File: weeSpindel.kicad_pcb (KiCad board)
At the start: 2 copper layers, 107.9 x 17.8 mm, 23 parts, among them J1 MPU-6050, SW1 POWER, U1 ESP-12E, U2 HT7733SA, U3 MCP1700-3302E_SOT23

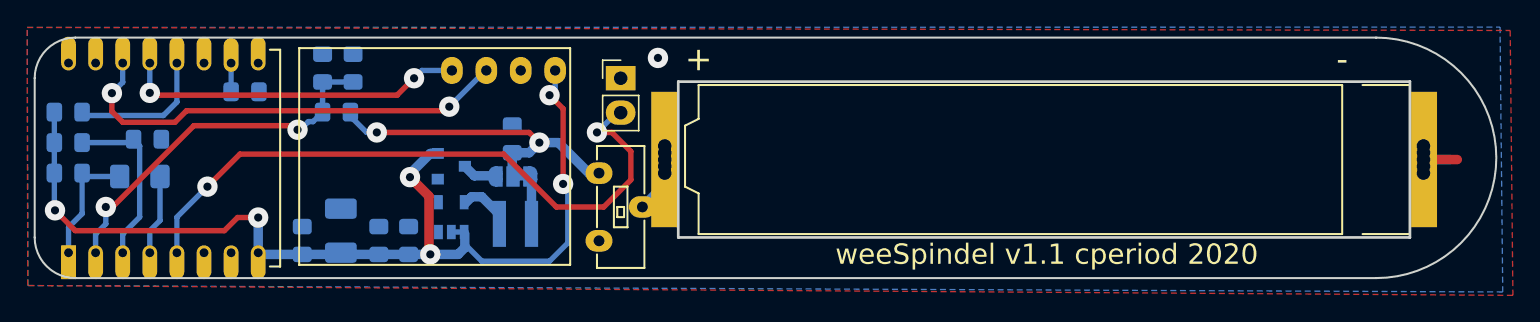
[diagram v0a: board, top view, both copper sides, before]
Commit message: the spring on the negative is a bit looser than necessary, allowing us to shave 2mm off our overall length
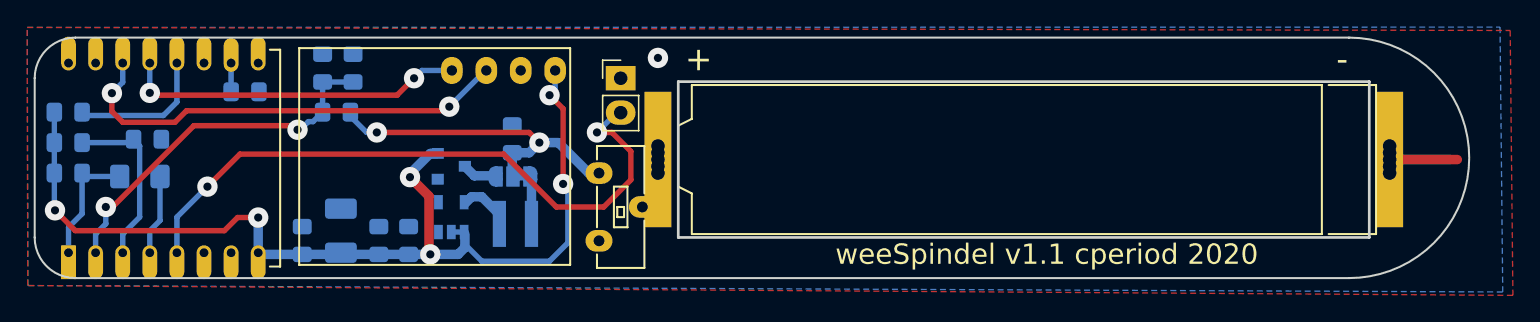
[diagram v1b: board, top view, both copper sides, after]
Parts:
- moved BT1 1.50 mm to (164.0, 105.0)
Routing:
- net GND: track 4.50 -> 9.71 mm
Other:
- board size 107.9 x 17.8 mm -> 105.9 x 17.8 mm
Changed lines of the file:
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@@
     (thickness 1.6)
     (drawings 16)
-    (tracks 139)
+    (tracks 140)
     (zones 0)
     (modules 23)
@@
     (add_net SDA)
   )
+  (module CPB:Battery_Springs_AAA (layer F.Cu)
+    (at 164 105)
+    (fp_text reference BT1 (at 30.5 0 90) (layer F.SilkS) hide
+      (effects (font (size 1 1) (thickness 0.15)))
+    )
+    (fp_text value NiMH (at 0 -9.271) (layer F.Fab)
+      (effects (font (size 1 1) (thickness 0.15)))
+    )
+    (fp_line (start 22 -5.5) (end -24.5 -5.5) (layer F.SilkS) (width 0.15))
+    (fp_line (start -24.5 -5.5) (end -24.5 -3) (layer F.SilkS) (width 0.15))
+    (fp_line (start -24.5 -3) (end -25.5 -2.5) (layer F.SilkS) (width 0.15))
+    (fp_line (start -25.5 -2.5) (end -25.5 2) (layer F.SilkS) (width 0.15))
+    (fp_line (start -25.5 2) (end -24.5 2.5) (layer F.SilkS) (width 0.15))
+    (fp_line (start -24.5 2.5) (end -24.5 5.5) (layer F.SilkS) (width 0.15))
+    (fp_line (start -24.5 5.5) (end 22 5.5) (layer F.SilkS) (width 0.15))
+    (fp_line (start 22 5.5) (end 22 -5.5) (layer F.SilkS) (width 0.15))
+    (fp_line (start 22.5 -5.5) (end 26 -5.5) (layer F.SilkS) (width 0.15))
+    (fp_line (start 26 -5.5) (end 26 5.5) (layer F.SilkS) (width 0.15))
+    (fp_line (start 26 5.5) (end 22.5 5.5) (layer F.SilkS) (width 0.15))
+    (fp_line (start 29 -6) (end -28.5 -6) (layer F.Fab) (width 0.15))
+    (fp_line (start -28.5 -6) (end -28.5 6) (layer F.Fab) (width 0.15))
+    (fp_line (start -28.5 6) (end 29 6) (layer F.Fab) (width 0.15))
+    (fp_line (start 29 6) (end 29 -6) (layer F.Fab) (width 0.15))
+    (pad 2 thru_hole circle (at 27 1) (size 1 1) (drill 1) (layers *.Cu *.Mask)
+      (net 1 GND))
+    (pad 2 thru_hole circle (at 27 0.5) (size 1 1) (drill 1) (layers *.Cu *.Mask)
+      (net 1 GND))
+    (pad 2 thru_hole circle (at 27 -1) (size 1 1) (drill 1) (layers *.Cu *.Mask)
+      (net 1 GND))
+    (pad 2 thru_hole circle (at 27 -0.5) (size 1 1) (drill 1) (layers *.Cu *.Mask)
+      (net 1 GND))
+    (pad 1 thru_hole circle (at -27 -0.5) (size 1 1) (drill 1) (layers *.Cu *.Mask)
+      (net 8 "Net-(BT1-Pad1)"))
+    (pad 1 thru_hole circle (at -27 0.5) (size 1 1) (drill 1) (layers *.Cu *.Mask)
+      (net 8 "Net-(BT1-Pad1)"))
+    (pad 1 thru_hole circle (at -27 1) (size 1 1) (drill 1) (layers *.Cu *.Mask)
+      (net 8 "Net-(BT1-Pad1)"))
+    (pad 1 thru_hole circle (at -27 -1) (size 1 1) (drill 1) (layers *.Cu *.Mask)
+      (net 8 "Net-(BT1-Pad1)"))
+    (pad 2 thru_hole rect (at 27 0) (size 2 10) (drill 1) (layers *.Cu *.Mask)
+      (net 1 GND))
+    (pad 1 thru_hole rect (at -27 0) (size 2 10) (drill 1) (layers *.Cu *.Mask)
+      (net 8 "Net-(BT1-Pad1)"))
+  )
   (module Jumper:SolderJumper-3_P1.3mm_Bridged12_RoundedPad1.0x1.5mm (layer B.Cu)
     (at 126.3 106.25 180)
@@
     )
   )
-  (module CPB:Battery_Springs_AAA (layer F.Cu)
-    (at 165.5 105)
-    (fp_text reference BT1 (at 30.5 0 90) (layer F.SilkS) hide
-      (effects (font (size 1 1) (thickness 0.15)))
-    )
-    (fp_text value NiMH (at 0 -9.271) (layer F.Fab)
-      (effects (font (size 1 1) (thickness 0.15)))
-    )
-    (fp_line (start 22 -5.5) (end -25.5 -5.5) (layer F.SilkS) (width 0.15))
-    (fp_line (start -25.5 -5.5) (end -25.5 -3) (layer F.SilkS) (width 0.15))
-    (fp_line (start -25.5 -3) (end -26.5 -2.5) (layer F.SilkS) (width 0.15))
-    (fp_line (start -26.5 -2.5) (end -26.5 2) (layer F.SilkS) (width 0.15))
-    (fp_line (start -26.5 2) (end -25.5 2.5) (layer F.SilkS) (width 0.15))
-    (fp_line (start -25.5 2.5) (end -25.5 5.5) (layer F.SilkS) (width 0.15))
-    (fp_line (start -25.5 5.5) (end 22 5.5) (layer F.SilkS) (width 0.15))
-    (fp_line (start 22 5.5) (end 22 -5.5) (layer F.SilkS) (width 0.15))
-    (fp_line (start 23.5 -5.5) (end 27 -5.5) (layer F.SilkS) (width 0.15))
-    (fp_line (start 27 -5.5) (end 27 5.5) (layer F.SilkS) (width 0.15))
-    (fp_line (start 27 5.5) (end 23.5 5.5) (layer F.SilkS) (width 0.15))
-    (fp_line (start 29.5 -6) (end -29.5 -6) (layer F.Fab) (width 0.15))
-    (fp_line (start -29.5 -6) (end -29.5 6) (layer F.Fab) (width 0.15))
-    (fp_line (start -29.5 6) (end 29.5 6) (layer F.Fab) (width 0.15))
-    (fp_line (start 29.5 6) (end 29.5 -6) (layer F.Fab) (width 0.15))
-    (pad 2 thru_hole circle (at 28 1) (size 1 1) (drill 1) (layers *.Cu *.Mask)
-      (net 1 GND))
-    (pad 2 thru_hole circle (at 28 0.5) (size 1 1) (drill 1) (layers *.Cu *.Mask)
-      (net 1 GND))
-    (pad 2 thru_hole circle (at 28 -1) (size 1 1) (drill 1) (layers *.Cu *.Mask)
-      (net 1 GND))
-    (pad 2 thru_hole circle (at 28 -0.5) (size 1 1) (drill 1) (layers *.Cu *.Mask)
-      (net 1 GND))
-    (pad 1 thru_hole circle (at -28 -0.5) (size 1 1) (drill 1) (layers *.Cu *.Mask)
-      (net 8 "Net-(BT1-Pad1)"))
-    (pad 1 thru_hole circle (at -28 0.5) (size 1 1) (drill 1) (layers *.Cu *.Mask)
-      (net 8 "Net-(BT1-Pad1)"))
-    (pad 1 thru_hole circle (at -28 1) (size 1 1) (drill 1) (layers *.Cu *.Mask)
-      (net 8 "Net-(BT1-Pad1)"))
-    (pad 1 thru_hole circle (at -28 -1) (size 1 1) (drill 1) (layers *.Cu *.Mask)
-      (net 8 "Net-(BT1-Pad1)"))
-    (pad 2 thru_hole rect (at 28 0) (size 2 10) (drill 1) (layers *.Cu *.Mask)
-      (net 1 GND))
-    (pad 1 thru_hole rect (at -28 0) (size 2 10) (drill 1) (layers *.Cu *.Mask)
-      (net 8 "Net-(BT1-Pad1)") (clearance 1))
-  )
   (module CPB:Socket_Strip_Straight_1x02_Oval_Pitch2.54mm (layer F.Cu)
     (at 134.25 99)
@@
   )
   (gr_line (start 138.5 110.75) (end 138.5 99.25) (layer Edge.Cuts) (width 0.2))
-  (gr_line (start 192.5 110.75) (end 138.5 110.75) (layer Edge.Cuts) (width 0.2))
-  (gr_line (start 192.5 99.25) (end 192.5 110.75) (layer Edge.Cuts) (width 0.2))
-  (gr_line (start 138.5 99.25) (end 192.5 99.25) (layer Edge.Cuts) (width 0.2))
-  (gr_line (start 190 96) (end 94 96) (layer Edge.Cuts) (width 0.15))
-  (gr_arc (start 190 104.875) (end 190 113.75) (angle -180) (layer Edge.Cuts) (width 0.15))
-  (gr_line (start 94 113.75) (end 190 113.75) (layer Edge.Cuts) (width 0.15))
+  (gr_line (start 189.5 110.75) (end 138.5 110.75) (layer Edge.Cuts) (width 0.2))
+  (gr_line (start 189.5 99.25) (end 189.5 110.75) (layer Edge.Cuts) (width 0.2))
+  (gr_line (start 138.5 99.25) (end 189.5 99.25) (layer Edge.Cuts) (width 0.2))
+  (gr_line (start 188 96) (end 94 96) (layer Edge.Cuts) (width 0.15))
+  (gr_arc (start 188 104.875) (end 188 113.75) (angle -180) (layer Edge.Cuts) (width 0.15))
+  (gr_line (start 94 113.75) (end 188 113.75) (layer Edge.Cuts) (width 0.15))
   (gr_arc (start 94 110.75) (end 91 110.75) (angle -90) (layer Edge.Cuts) (width 0.15))
   (gr_line (start 91 99) (end 91 110.75) (layer Edge.Cuts) (width 0.15))
@@
     (effects (font (size 1.5 1.5) (thickness 0.3)))
   )
-  (segment (start 193.5 105) (end 195.5 105) (width 0.7) (layer B.Cu) (net 1))
-  (segment (start 193.5 105) (end 196 105) (width 0.7) (layer F.Cu) (net 1))
   (via (at 137 97.5) (size 1.5) (drill 0.6) (layers F.Cu B.Cu) (net 1))
+  (segment (start 191.5 105) (end 195.5 105) (width 0.7) (layer B.Cu) (net 1))
+  (segment (start 191 104.5) (end 191.5 105) (width 0.7) (layer B.Cu) (net 1))
+  (segment (start 191 105) (end 196 105) (width 0.7) (layer F.Cu) (net 1))
   (via (at 107.497 109.279) (size 1.5) (drill 0.6) (layers F.Cu B.Cu) (net 2))
   (segment (start 107.497 109.279) (end 107.497 111.879) (width 0.7) (layer B.Cu) (net 2) (status 20))

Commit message: a bit of simplifying. We almost certainly don't need that jumper.
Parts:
- removed JP2: REGULATOR, Jumper:SolderJumper-3_P1.3mm_Bridged12_RoundedPad1.0x1.5mm
- moved R1 4.11 mm to (115.8, 98.2), turned to 270 degrees
- moved C2 3.48 mm to (124.5, 106.5), turned to 180 degrees
- moved U3 2.46 mm to (119.5, 106.5), turned to 180 degrees
- moved C1 1.25 mm to (109.5, 111.0)
- moved C5 1.10 mm to (112.5, 110.2)
- moved C6 1.00 mm to (111.2, 98.2)
- moved R2 1.00 mm to (113.5, 98.2)
- moved U2 0.98 mm to (122.0, 110.2), turned to 0 degrees
- moved C4 0.90 mm to (115.5, 111.0)
- moved C3 0.85 mm to (117.8, 111.0)
- moved L1 0.58 mm to (127.0, 110.0), turned to 270 degrees
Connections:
- L1 pad 1: Net-(JP2-Pad1) -> Net-(C2-Pad1)
- U3 pad 3: Net-(JP2-Pad3) -> Net-(C2-Pad1)
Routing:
- net 3V3: track 75.5 -> 81.5 mm, vias 6 -> 3
- net Net-(JP2-Pad1): track 3.50 -> 0.00 mm
- net Net-(C2-Pad1): track 25.7 -> 29.0 mm, vias 2 -> 3
- net ADC: track 27.3 -> 30.4 mm
- net Net-(JP1-Pad2): track 48.0 -> 45.3 mm
- net Net-(JP2-Pad3): track 2.44 -> 0.00 mm
- net SCL: track 33.5 -> 35.7 mm
- net SDA: track 25.3 -> 26.6 mm
- net Net-(L1-Pad2): track 4.52 -> 3.38 mm
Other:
- board text added: "weeSpindel v1.2 cperiod 2020"
- board text removed: "weeSpindel v1.1 cperiod 2020"

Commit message: more trace cleanups.
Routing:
- net Net-(JP1-Pad2): track 45.3 -> 41.6 mm
- net 3V3: track 81.5 -> 80.3 mm
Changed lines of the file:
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@@
     (thickness 1.6)
     (drawings 16)
-    (tracks 138)
+    (tracks 136)
     (zones 0)
     (modules 22)
@@
   (segment (start 107.497 111.879) (end 107.497 110.747) (width 0.4) (layer B.Cu) (net 2))
   (segment (start 107.497 110.747) (end 106.5 109.75) (width 0.4) (layer B.Cu) (net 2))
-  (segment (start 129 100.25) (end 130 101.25) (width 0.4) (layer F.Cu) (net 2))
-  (segment (start 129.2 108) (end 106.5 108) (width 0.4) (layer F.Cu) (net 2))
-  (segment (start 130 107.2) (end 129.2 108) (width 0.4) (layer F.Cu) (net 2))
-  (segment (start 130 101.25) (end 130 107.2) (width 0.4) (layer F.Cu) (net 2))
   (segment (start 98.5 110.25) (end 94 110.25) (width 0.4) (layer F.Cu) (net 2))
   (segment (start 102.15 106.6) (end 98.5 110.25) (width 0.4) (layer F.Cu) (net 2))
@@
   (segment (start 105.2 106.6) (end 102.15 106.6) (width 0.4) (layer F.Cu) (net 2))
   (segment (start 106.5 107.9) (end 105.2 106.6) (width 0.4) (layer F.Cu) (net 2))
+  (segment (start 128.1 108) (end 106.5 108) (width 0.4) (layer F.Cu) (net 2))
+  (segment (start 129.3 106.8) (end 128.1 108) (width 0.4) (layer F.Cu) (net 2))
+  (segment (start 129 100.25) (end 129.3 100.55) (width 0.4) (layer F.Cu) (net 2))
+  (segment (start 129.3 100.55) (end 129.3 106.8) (width 0.4) (layer F.Cu) (net 2))
   (segment (start 95.497 110.503) (end 95.497 111.879) (width 0.4) (layer B.Cu) (net 3))
   (segment (start 96.25 109.75) (end 95.497 110.503) (width 0.4) (layer B.Cu) (net 3))
@@
   (segment (start 101.497 110.703) (end 101.497 111.879) (width 0.4) (layer B.Cu) (net 7))
   (via (at 103.6 108.6) (size 1.5) (drill 0.6) (layers F.Cu B.Cu) (net 7))
-  (segment (start 133.6 103) (end 132.5 103) (width 0.4) (layer F.Cu) (net 7))
-  (segment (start 135 104.4) (end 133.6 103) (width 0.4) (layer F.Cu) (net 7))
-  (segment (start 105.2 110.2) (end 130.3 110.2) (width 0.4) (layer F.Cu) (net 7))
+  (segment (start 130.3 104) (end 131.3 103) (width 0.4) (layer F.Cu) (net 7))
+  (segment (start 130.3 108.3) (end 130.3 104) (width 0.4) (layer F.Cu) (net 7))
+  (segment (start 128.4 110.2) (end 130.3 108.3) (width 0.4) (layer F.Cu) (net 7))
   (segment (start 103.6 108.6) (end 105.2 110.2) (width 0.4) (layer F.Cu) (net 7))
-  (segment (start 132 108.5) (end 133 108.5) (width 0.4) (layer F.Cu) (net 7))
-  (segment (start 130.3 110.2) (end 132 108.5) (width 0.4) (layer F.Cu) (net 7))
-  (segment (start 133 108.5) (end 135 106.5) (width 0.4) (layer F.Cu) (net 7))
-  (segment (start 135 106.5) (end 135 104.4) (width 0.4) (layer F.Cu) (net 7))
+  (segment (start 131.3 103) (end 132.5 103) (width 0.4) (layer F.Cu) (net 7))
+  (segment (start 105.2 110.2) (end 128.4 110.2) (width 0.4) (layer F.Cu) (net 7))
   (segment (start 137.5 106.85) (end 137.5 105) (width 0.7) (layer B.Cu) (net 8))
   (segment (start 135.85 108.5) (end 137.5 106.85) (width 0.7) (layer B.Cu) (net 8))
@@
   (segment (start 127 108.75) (end 126.5 108.75) (width 0.7) (layer B.Cu) (net 14))
   (segment (start 126.5 108.75) (end 125.55 107.8) (width 0.7) (layer B.Cu) (net 14))
-  (segment (start 115.75 100.5) (end 115.75 99.25) (width 0.4) (layer B.Cu) (net 14) (status 1000000))
-  (segment (start 115.75 100.5) (end 117.75 102.5) (width 0.4) (layer F.Cu) (net 14) (status 1000000))
-  (segment (start 117.75 102.5) (end 117.75 106.25) (width 0.4) (layer F.Cu) (net 14) (status 1000000))
-  (via (at 115.75 100.5) (size 1.5) (drill 0.6) (layers F.Cu B.Cu) (net 14) (status 1000000))
+  (segment (start 115.75 100.5) (end 115.75 99.25) (width 0.4) (layer B.Cu) (net 14))
+  (segment (start 115.75 100.5) (end 117.75 102.5) (width 0.4) (layer F.Cu) (net 14))
+  (segment (start 117.75 102.5) (end 117.75 106.25) (width 0.4) (layer F.Cu) (net 14))
+  (via (at 115.75 100.5) (size 1.5) (drill 0.6) (layers F.Cu B.Cu) (net 14))
   (via (at 117.75 106.25) (size 1.5) (drill 0.6) (layers F.Cu B.Cu) (net 14))
   (segment (start 117.75 106.25) (end 118 106.5) (width 0.7) (layer B.Cu) (net 14))
